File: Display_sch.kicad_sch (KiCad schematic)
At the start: 67 parts, among them J5 Conn_01x02_Male, U10 74HC595, U11 74HC595, U12 74HC595, U13 74HC595, U14 74HC595, U9 74HC595

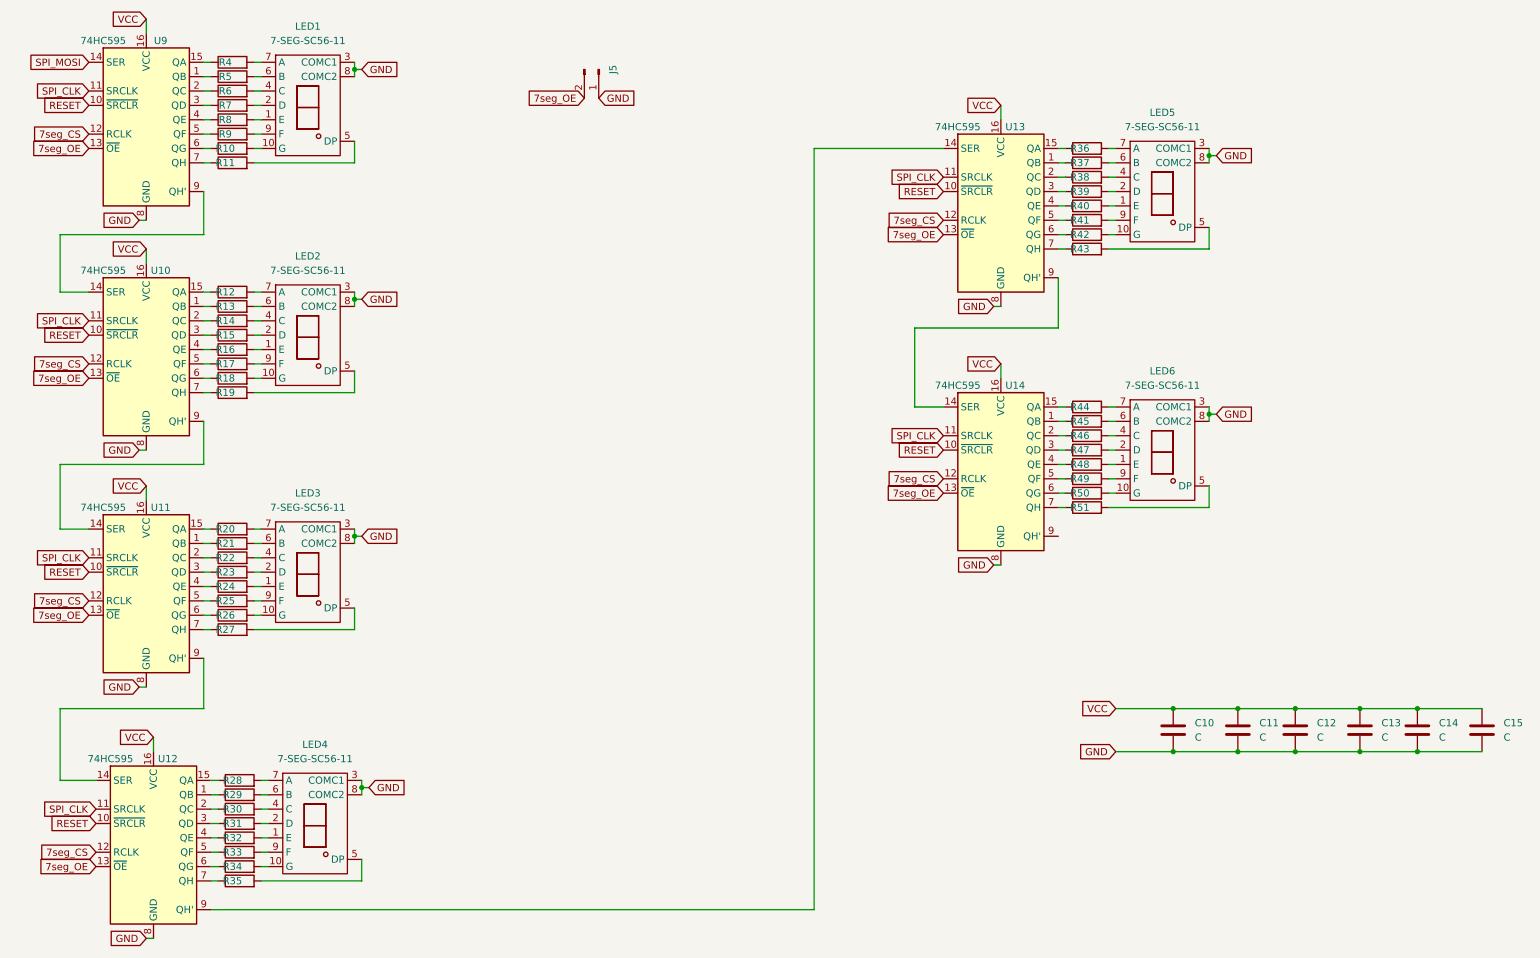
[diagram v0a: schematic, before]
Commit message: Tidy up of track routing to give more clearance. Tidy up missing silkscreen of chip numbers.
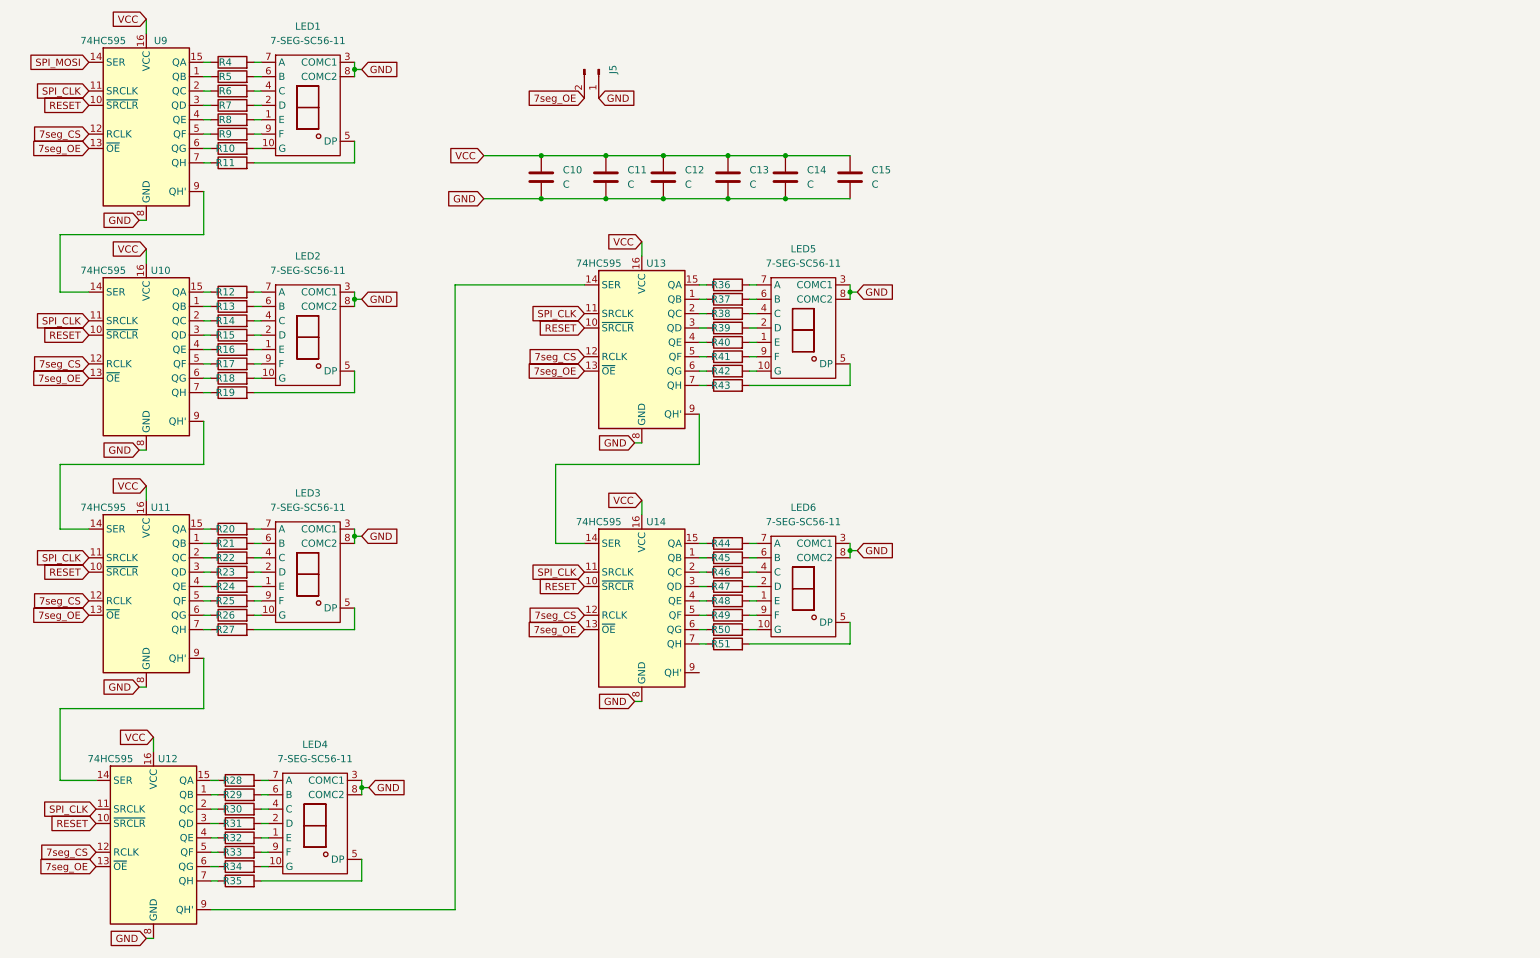
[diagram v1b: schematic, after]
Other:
- moved on the sheet: C10, C11, C12, C13, C14, C15, LED5, LED6, R36, R37, R38, R39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

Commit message: Version 1.2
Improved reset.
Added connection for PWM display brightness.

NOTE: This board revision is yet to be made and tested.
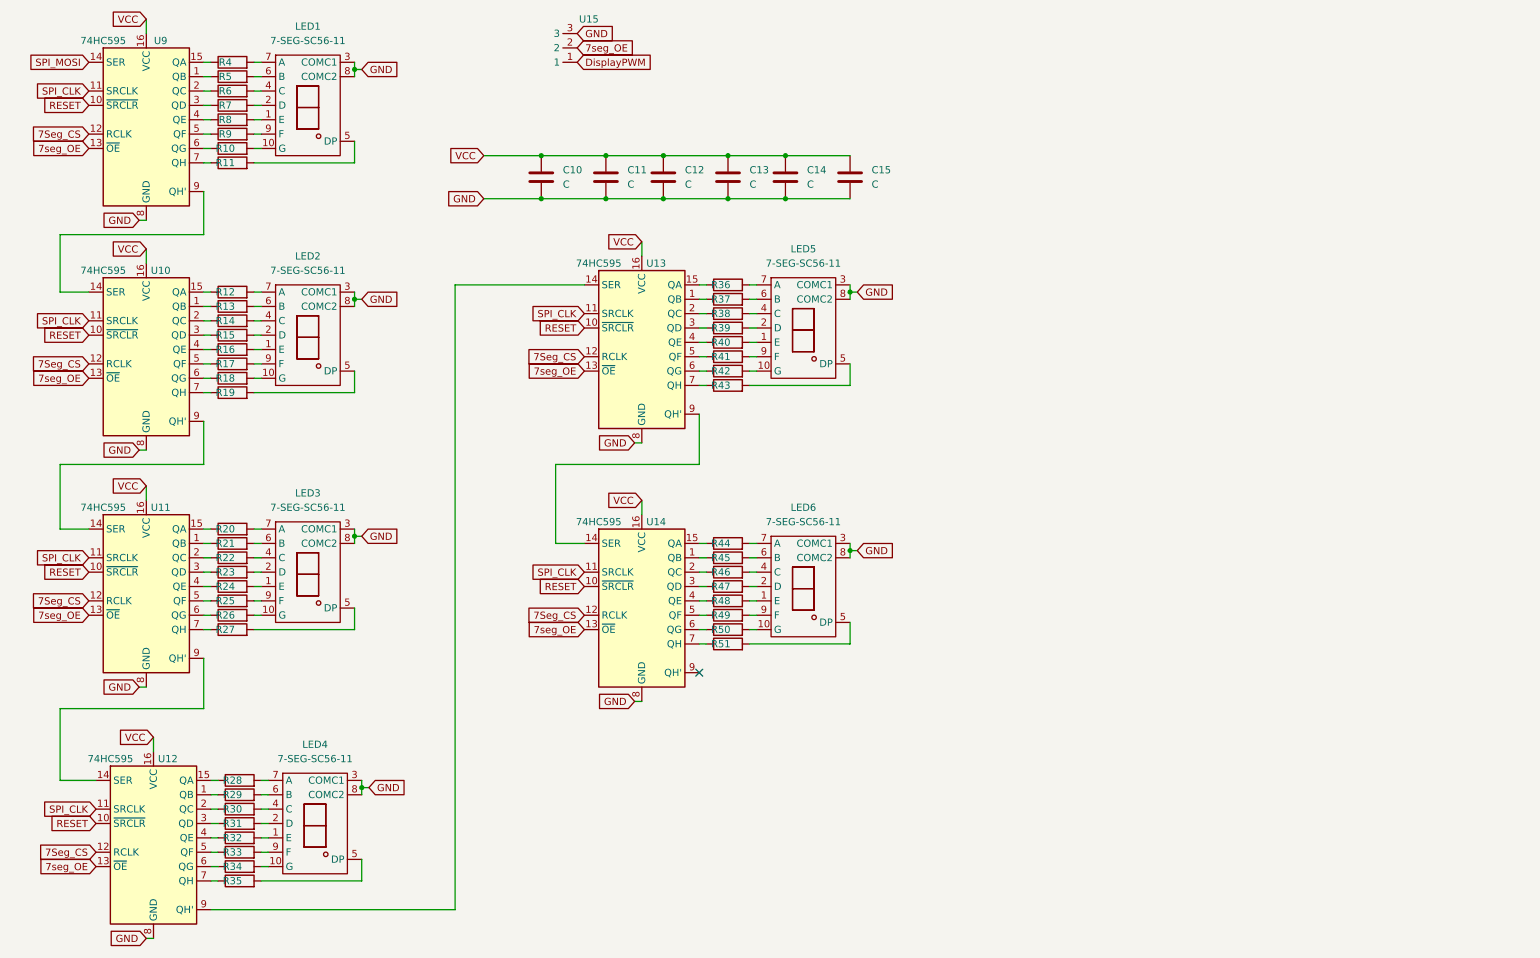
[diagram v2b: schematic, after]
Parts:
- removed J5: Conn_01x02_Male, Alius_6502:2_pin_header, symbol Connector:Conn_01x02_Male
- added U15: ~, Alius_6502:3_pin_header, symbol Alius:1*3_pin_header
- C10, C11, C12, C13, C14, C15: footprint Capacitor_THT:C_Axial_L3.8mm_D2.6mm_P7.50mm_Horizontal -> Alius_6502:C_Axial_L3.8mm_D2.6mm_P7.50mm_Horizontal
- LED1, LED2, LED3, LED4, LED5, LED6: footprint Alius_6502:7-SEG-SC56-11 -> Alius_6502:7-seg
- U10, U11, U12, U13, U14, U9: footprint Package_DIP:DIP-16_W7.62mm_LongPads -> Alius_6502:DIP-16_W7.62mm_LongPads
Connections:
- net 7seg_OE: now also U15.2
- net GND: now also U15.3
- net 7seg_CS renamed 7Seg_CS
- new net DisplayPWM: U15.1
- no-connect marks 0 -> 1
